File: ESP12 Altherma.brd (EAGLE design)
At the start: 89 x 49.8 mm, 58 parts, among them J1 455-1750-1-ND, K1 HRS1KH-S_DC5V, K2 HRS1KH-S_DC5V, U1 TLP291-4(GB-TP,E), U2 AP2112K-3.3TRG1, U4 DRDC3105E6-7, U5 SN74LVC1G125GV

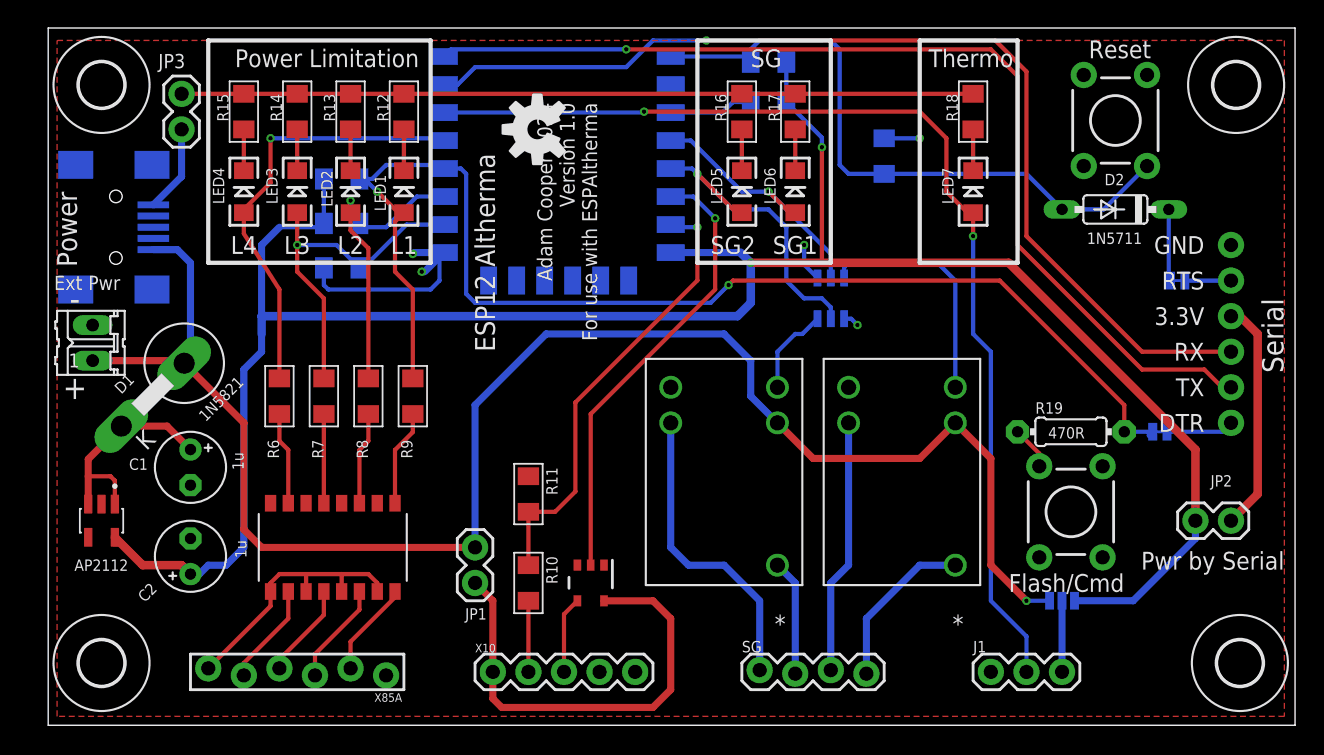
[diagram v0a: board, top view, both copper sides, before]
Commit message: shorten board. share GPIO for LP and SG. use JST connectors. tidy needless complexity
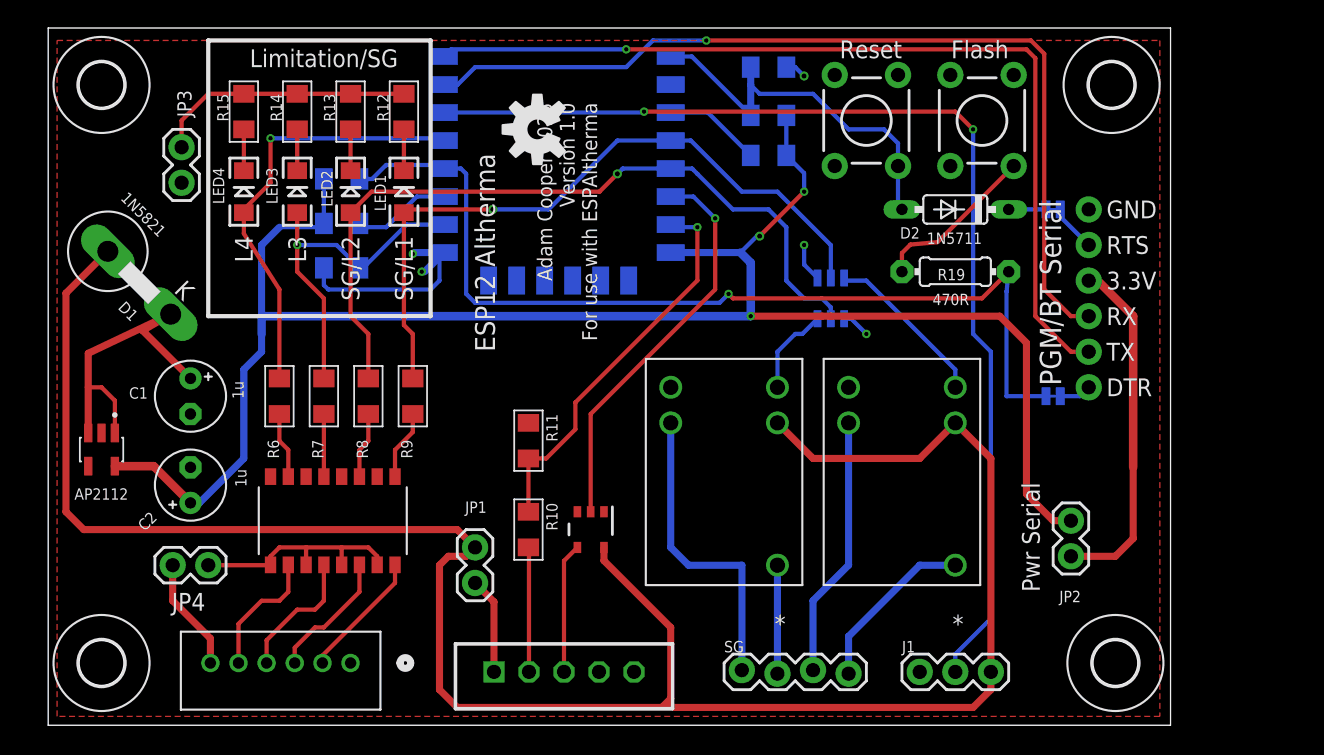
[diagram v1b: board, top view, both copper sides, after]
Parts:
- removed EP1: Ext Pwr, con-amp-quick:02P
- removed EP3: (no value), Master 2016:FCI_USB_B_SMD
- removed LED5, LED6, LED7: (no value), Master 2016:LED-1206
- removed R16, R17, R18: 180R, Master 2016:1206
- removed SJ1: 3V3 | 5V, Master 2016:SJ_3
- removed X10: (no value), SparkFun-Connectors:1X05
- removed X85A: (no value), SparkFun-Connectors:1X06_FEMALE_LOCK.010
- added J2: X85A - PL, conn-jst-pa6:CONN_B06B-PASK_JST
- added JP4: PL En, SparkFun-Passives:1X02
- added P1: X10A, con-jst-eh:B5B-EH-A
- JP2: value Pwr by Serial -> Pwr Serial
- S2: value Flash/Cmd -> Flash
- SV1: value Serial -> PGM/BT Serial
- moved S2 28.7 mm to (66.7, 43.2), turned to 90 degrees
- moved S1 17.8 mm to (58.4, 43.2)
- moved R19 14.1 mm to (64.8, 32.4)
- moved JP2 11.7 mm to (73.0, 12.1), turned to 90 degrees
- moved D2 11.4 mm to (64.8, 36.8)
- moved SV1 10.5 mm to (74.3, 36.8)
- moved C3 10.4 mm to (51.4, 47.0), turned to 180 degrees
- moved SJ3 10.2 mm to (71.8, 36.8)
- moved D1 9.67 mm to (4.26, 33.8), turned to 135 degrees
- moved H3 8.89 mm to (76.2, 4.45)
- moved H1 8.89 mm to (75.9, 45.7)
- moved SJ2 8.03 mm to (71.8, 23.5)
- moved J1 5.08 mm to (62.2, 3.81)
- moved C1 5.08 mm to (10.2, 23.5)
- moved C2 5.08 mm to (10.2, 17.1)
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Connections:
- removed net N$28: J1.3, SJ1.2
- removed net N$30: LED6.C, R17.2
- removed net N$31: LED7.C, R18.2
- net 5V: now also J1.3, U5.5; no longer EP1.1, EP3.VCC, SJ1.3
- net 5V_HP: now also P1.1; no longer U5.5, X10.1
- net GND: now also P1.5; no longer EP1.2, EP3.GND, X10.5
- net GPIO0: no longer LED1.A, R9.2
- net GPIO14: now also LED2.A, R8.2; no longer LED5.A
- net GPIO16: now also LED1.A, R9.2; no longer LED6.A
- net GPIO2: no longer LED2.A, R8.2
- net GPIO5: no longer LED7.A
- net N$11: now also J2.5; no longer X85A.5
- net N$12: now also J2.4; no longer X85A.4
- net N$13: now also J2.2; no longer X85A.2
- net N$20: now also P1.3; no longer X10.3
- net N$21: now also P1.2; no longer X10.2
- net N$27: now also J2.6, JP4.1; no longer LED5.C, R16.2
- net N$3: now also J2.3; no longer X85A.3
- net N$4: no longer R16.1, R17.1, R18.1
- net VCC: no longer SJ1.1
- net X85_GND: now also JP4.2; no longer X85A.6
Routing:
- net N$4: track 56.5 -> 18.6 mm
- net 5V: track 116.9 -> 151.0 mm, vias 1 -> 0
- net GPIO14: track 22.9 -> 55.1 mm
- net GPIO16: track 19.0 -> 50.2 mm
- net VCC: track 155.5 -> 127.9 mm, vias 2 -> 3
- net 5V_HP: track 32.6 -> 6.91 mm
- net GPIO0: track 89.6 -> 68.8 mm, vias 2 -> 1
- net RST: track 46.5 -> 28.0 mm
- net GPIO2: track 22.2 -> 7.04 mm, vias 1 -> 0
- net N$1: track 3.11 -> 11.8 mm
- net N$9: track 16.6 -> 25.1 mm
- net RXD: track 73.6 -> 65.4 mm
- net N$8: track 15.9 -> 24.0 mm
- net TXD: track 73.5 -> 66.0 mm
- net GND: track 28.9 -> 22.6 mm
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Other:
- board size 89 x 49.8 mm -> 80.1 x 49.8 mm
- board text added: "Adam Cooper 2025 Version 1.0 For use with ESPAltherma"
- board text added: "Limitation/SG"
- board text added: "SG/L1"
- board text added: "SG/L2"
- board text removed: "+"
- board text removed: "-"
- board text removed: "Adam Cooper 2024 Version 1.0 For use with ESPAltherma"
- board text removed: "L1"
- board text removed: "L2"
- board text removed: "Power"
- board text removed: "Power Limitation"
- board text removed: "SG"
- board text removed: "SG1"
- board text removed: "SG2"
- board text removed: "Thermo"

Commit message: change esp12 to version without Restrict layer so I can panelise
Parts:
- SJR1: device esp12e:ESP8266-ESP12E -> esp12e:ESP8266-ESP12E0-NKE
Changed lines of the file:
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@@
 <layer number="37" name="tTest" color="7" fill="1" visible="no" active="yes"/>
 <layer number="38" name="bTest" color="7" fill="1" visible="no" active="yes"/>
-<layer number="39" name="tKeepout" color="4" fill="11" visible="yes" active="yes"/>
-<layer number="40" name="bKeepout" color="1" fill="11" visible="yes" active="yes"/>
-<layer number="41" name="tRestrict" color="4" fill="10" visible="yes" active="yes"/>
-<layer number="42" name="bRestrict" color="1" fill="10" visible="yes" active="yes"/>
-<layer number="43" name="vRestrict" color="2" fill="10" visible="yes" active="yes"/>
+<layer number="39" name="tKeepout" color="4" fill="11" visible="no" active="yes"/>
+<layer number="40" name="bKeepout" color="1" fill="11" visible="no" active="yes"/>
+<layer number="41" name="tRestrict" color="4" fill="10" visible="no" active="yes"/>
+<layer number="42" name="bRestrict" color="1" fill="10" visible="no" active="yes"/>
+<layer number="43" name="vRestrict" color="2" fill="10" visible="no" active="yes"/>
 <layer number="44" name="Drills" color="7" fill="1" visible="no" active="yes"/>
-<layer number="45" name="Holes" color="7" fill="1" visible="no" active="yes"/>
-<layer number="46" name="Milling" color="3" fill="1" visible="yes" active="yes"/>
+<layer number="45" name="Holes" color="7" fill="1" visible="yes" active="yes"/>
+<layer number="46" name="Milling" color="3" fill="1" visible="no" active="yes"/>
 <layer number="47" name="Measures" color="7" fill="1" visible="no" active="yes"/>
 <layer number="48" name="Document" color="7" fill="1" visible="no" active="yes"/>
 <layer number="49" name="Reference" color="7" fill="1" visible="no" active="yes"/>
 <layer number="50" name="dxf" color="7" fill="1" visible="no" active="no"/>
-<layer number="51" name="tDocu" color="6" fill="1" visible="no" active="yes"/>
+<layer number="51" name="tDocu" color="6" fill="1" visible="yes" active="yes"/>
 <layer number="52" name="bDocu" color="7" fill="1" visible="no" active="yes"/>
 <layer number="53" name="tGND_GNDA" color="7" fill="9" visible="no" active="no"/>
@@
 </groups>
 <elements>
-<element name="SJR1" library="esp12e" package="ESP8266-ESP12E" value="" x="36.83" y="41.91" smashed="yes" rot="MR0">
+<element name="SJR1" library="esp12e" package="ESP8266-ESP12E0-NKE" value="" x="36.83" y="41.91" smashed="yes" rot="MR0">
 <attribute name="NAME" x="39.45" y="33.75" size="1.27" layer="52" rot="MR90"/>
 </element>
@@
 <element name="JP3" library="SparkFun-Passives" package="1X02" value="Signals" x="9.525" y="41.275" smashed="yes" rot="R270">
 <attribute name="NAME" x="10.2362" y="43.4213" size="1.016" layer="25" ratio="10" rot="R90"/>
-<attribute name="VALUE" x="4.445" y="35.56" size="1.27" layer="51"/>
 </element>
 <element name="C2" library="Master 2016" package="E2,5-5" value="1u" x="10.16" y="17.145" smashed="yes" rot="R90">

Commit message: Provisionally final tweaks prior to attempting panelisation
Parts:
- added JP5: SG En, SparkFun-Passives:1X02
- J1: value 455-1750-1-ND -> Thermo Rly
- JP3: value Signals -> LED En
- moved LOGO1 14.7 mm to (49.5, 40.6), turned to 0 degrees
- moved R11 2.54 mm to (34.3, 17.8), turned to 0 degrees
- moved JP1 1.27 mm to (30.5, 14.0)
- moved R10 1.27 mm to (34.3, 12.7)
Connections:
- new net N$6: JP5.1, K1.2, K2.2
- net 5V: now also JP5.2; no longer K1.2, K2.2
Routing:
- net N$6: track 0.00 -> 35.5 mm
- net 5V: track 151.0 -> 131.4 mm
- net GPIO13: track 28.0 -> 33.0 mm
- net GPIO12: track 28.5 -> 30.7 mm
- net N$21: track 8.91 -> 7.64 mm
- net 5V_HP: track 6.91 -> 8.18 mm

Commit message: I think this is v1.0. This commit free of any panelisation guff.
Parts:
- removed SG: (no value), SparkFun-Connectors:1X04_LOCK
- removed SJ3: SOLDERJUMPERTRACE, Master 2016:SJ_2S-TRACE
- added CONN4: SG, SparkFun-Connectors:1X04
- added LED5: (no value), Master 2016:LED-1206
- added R17: 180R, Master 2016:1206
- added SJ1: SOLDERJUMPERTRACE, Master 2016:SJ_2S-TRACE
- U1: value TLP291-4(GB-TP,E) -> TLP291-4
- U2: value AP2112K-3.3TRG1 -> AP2112K-3.3
- moved D2 0.63 mm to (64.8, 36.2)
- moved S1 0.63 mm to (58.4, 43.8)
- moved S2 0.63 mm to (66.7, 43.8)
- renumbered J1 to CON5, J2 to CON2, P1 to CON3, R19 to R16, SV1 to CON1
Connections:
- new net N$28: LED5.C, R17.2
- net GPIO2: now also R17.1
- net N$14: now also SJ1.1; no longer SJ3.1
- net N$22: now also CONN4.1; no longer SG.1
- net N$23: now also CONN4.2; no longer SG.2
- net N$24: now also CONN4.3; no longer SG.3
- net N$25: now also CONN4.4; no longer SG.4
- net N$5: now also SJ1.2; no longer SJ3.2
- net VCC: now also LED5.A
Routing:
- net VCC: track 127.6 -> 144.2 mm
- net GPIO2: track 7.04 -> 15.3 mm, vias 0 -> 1
- net GPIO0: track 68.8 -> 63.5 mm
- net RXD: track 65.4 -> 60.1 mm
- net N$28: track 0.00 -> 3.58 mm
- net TXD: track 66.0 -> 62.6 mm
- net N$22: track 22.0 -> 19.9 mm
- net GND: track 22.6 -> 21.8 mm
- net N$5: track 3.38 -> 2.67 mm
- net RST: track 28.0 -> 28.6 mm
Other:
- board text added: "1"
- board text added: "5V"
- board text added: "G"
- board text added: "OK"
- board text added: "SG1"
- board text added: "SG2"
- board text added: "Sig"
- board text added: "Smart Gd"
- board text removed: "AP2112"
- board text removed: "C1"
- board text removed: "C2"
- board text removed: "C3"
- board text removed: "D1"
- board text removed: "D2"
- board text removed: "EP1"
- board text removed: "EP2"
- board text removed: "JP1"
- board text removed: "JP2"
- board text removed: "JP3"
- board text removed: "JP4"
- board text removed: "JP5"
- board text removed: "JP6"
- board text removed: "JP7"
- board text removed: "JP8"
- board text removed: "JP9"
- board text removed: "LED1"
- board text removed: "LED2"
- board text removed: "Q1"
- board text removed: "R1"
- board text removed: "R10"
- board text removed: "R11"
- board text removed: "R12"
- board text removed: "R2"
- board text removed: "R3"
- board text removed: "R4"
- board text removed: "R5"
- board text removed: "R6"
- board text removed: "R7"
- board text removed: "R8"
- board text removed: "R9"
- board text removed: "S1"
- board text removed: "S2"
- board text removed: "SJ1"
- board text removed: "SJ2"
- board text removed: "SJ3"
- board text removed: "SJR1"
- board text removed: "U$1"
- board text removed: "U2"
